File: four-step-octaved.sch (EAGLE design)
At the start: 29 parts, among them IC1 556, IC2 4017N, IC3 4040N, U1 LM386N

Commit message: Tighten
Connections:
- net +9V: no longer C4.1
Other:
- moved on the sheet: C4, IC2P, IC3, R1, RV1
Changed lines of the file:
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@@
 <instance part="IC1" gate="G$1" x="10.16" y="81.28"/>
 <instance part="IC2" gate="A" x="81.28" y="76.2"/>
-<instance part="IC3" gate="A" x="243.84" y="91.44"/>
+<instance part="IC3" gate="A" x="215.9" y="76.2"/>
 <instance part="U1" gate="G1" x="248.92" y="63.5"/>
 <instance part="SUPPLY1" gate="G$1" x="-25.4" y="101.6"/>
 <instance part="GND1" gate="1" x="-5.08" y="12.7"/>
-<instance part="R1" gate="G$1" x="-48.26" y="86.36"/>
+<instance part="R1" gate="G$1" x="-43.18" y="86.36"/>
 <instance part="R2" gate="G$1" x="-15.24" y="81.28" rot="R270"/>
 <instance part="R3" gate="G$1" x="35.56" y="81.28" rot="R90"/>
-<instance part="RV1" gate="G$1" x="-35.56" y="86.36" rot="R270"/>
+<instance part="RV1" gate="G$1" x="-30.48" y="86.36" rot="R270"/>
 <instance part="C1" gate="G$1" x="-15.24" y="68.58"/>
 <instance part="C2" gate="G$1" x="43.18" y="73.66"/>
@@
 <instance part="D7" gate="G$1" x="132.08" y="43.18"/>
 <instance part="D8" gate="G$1" x="154.94" y="35.56" rot="MR270"/>
-<instance part="IC2" gate="P" x="55.88" y="88.9" smashed="yes">
+<instance part="IC2" gate="P" x="60.96" y="86.36" smashed="yes">
 <attribute name="NAME" x="59.69" y="85.725" size="1.778" layer="95" rot="R90"/>
 </instance>
-<instance part="C4" gate="G$1" x="63.5" y="91.44"/>
+<instance part="C4" gate="G$1" x="66.04" y="86.36"/>
 </instances>
 <busses>
@@
 <pinref part="RV1" gate="G$1" pin="E"/>
 <wire x1="-2.54" y1="86.36" x2="-15.24" y2="86.36" width="0.1524" layer="91"/>
-<wire x1="-15.24" y1="86.36" x2="-27.94" y2="86.36" width="0.1524" layer="91"/>
-<wire x1="-27.94" y1="86.36" x2="-27.94" y2="81.28" width="0.1524" layer="91"/>
-<junction x="-27.94" y="86.36"/>
+<wire x1="-15.24" y1="86.36" x2="-22.86" y2="86.36" width="0.1524" layer="91"/>
+<wire x1="-22.86" y1="86.36" x2="-22.86" y2="81.28" width="0.1524" layer="91"/>
+<junction x="-22.86" y="86.36"/>
 <pinref part="RV1" gate="G$1" pin="S"/>
-<wire x1="-27.94" y1="81.28" x2="-35.56" y2="81.28" width="0.1524" layer="91"/>
+<wire x1="-22.86" y1="81.28" x2="-30.48" y2="81.28" width="0.1524" layer="91"/>
 <pinref part="R2" gate="G$1" pin="1"/>
 <junction x="-15.24" y="86.36"/>
@@
 <segment>
 <pinref part="SUPPLY1" gate="G$1" pin="+9V"/>
-<wire x1="-25.4" y1="99.06" x2="-58.42" y2="99.06" width="0.1524" layer="91"/>
-<wire x1="-58.42" y1="99.06" x2="-58.42" y2="86.36" width="0.1524" layer="91"/>
+<wire x1="-25.4" y1="99.06" x2="-50.8" y2="99.06" width="0.1524" layer="91"/>
+<wire x1="-50.8" y1="99.06" x2="-50.8" y2="86.36" width="0.1524" layer="91"/>
 <pinref part="R1" gate="G$1" pin="1"/>
-<wire x1="-58.42" y1="86.36" x2="-53.34" y2="86.36" width="0.1524" layer="91"/>
+<wire x1="-50.8" y1="86.36" x2="-48.26" y2="86.36" width="0.1524" layer="91"/>
 <pinref part="IC1" gate="G$1" pin="RST"/>
 <wire x1="-2.54" y1="78.74" x2="-7.62" y2="78.74" width="0.1524" layer="91"/>
@@
 <wire x1="43.18" y1="88.9" x2="43.18" y2="78.74" width="0.1524" layer="91"/>
 <junction x="25.4" y="88.9"/>
+<wire x1="25.4" y1="99.06" x2="60.96" y2="99.06" width="0.1524" layer="91"/>
+<junction x="25.4" y="99.06"/>
 <pinref part="IC2" gate="P" pin="VDD"/>
-<wire x1="25.4" y1="99.06" x2="55.88" y2="99.06" width="0.1524" layer="91"/>
-<wire x1="55.88" y1="99.06" x2="55.88" y2="96.52" width="0.1524" layer="91"/>
-<junction x="25.4" y="99.06"/>
-<pinref part="C4" gate="G$1" pin="1"/>
-<wire x1="63.5" y1="96.52" x2="55.88" y2="96.52" width="0.1524" layer="91"/>
-<junction x="55.88" y="96.52"/>
+<wire x1="60.96" y1="99.06" x2="60.96" y2="93.98" width="0.1524" layer="91"/>
 </segment>
 </net>
@@
 <pinref part="IC1" gate="G$1" pin="GND"/>
 <wire x1="-2.54" y1="71.12" x2="-5.08" y2="71.12" width="0.1524" layer="91"/>
-<wire x1="-5.08" y1="71.12" x2="-5.08" y2="60.96" width="0.1524" layer="91"/>
 <pinref part="GND1" gate="1" pin="GND"/>
-<pinref part="C1" gate="G$1" pin="-"/>
-<wire x1="-5.08" y1="60.96" x2="-5.08" y2="25.4" width="0.1524" layer="91"/>
+<wire x1="-5.08" y1="71.12" x2="-5.08" y2="25.4" width="0.1524" layer="91"/>
 <wire x1="-5.08" y1="25.4" x2="-5.08" y2="15.24" width="0.1524" layer="91"/>
-<wire x1="-15.24" y1="63.5" x2="-15.24" y2="60.96" width="0.1524" layer="91"/>
-<wire x1="-15.24" y1="60.96" x2="-5.08" y2="60.96" width="0.1524" layer="91"/>
-<junction x="-5.08" y="60.96"/>
-<pinref part="C3" gate="G$1" pin="2"/>
-<wire x1="35.56" y1="63.5" x2="35.56" y2="60.96" width="0.1524" layer="91"/>
-<wire x1="35.56" y1="60.96" x2="-5.08" y2="60.96" width="0.1524" layer="91"/>
-<junction x="-5.08" y="60.96"/>
-<pinref part="C2" gate="G$1" pin="2"/>
-<wire x1="43.18" y1="71.12" x2="43.18" y2="60.96" width="0.1524" layer="91"/>
-<wire x1="43.18" y1="60.96" x2="35.56" y2="60.96" width="0.1524" layer="91"/>
-<junction x="35.56" y="60.96"/>
 <pinref part="R4" gate="G$1" pin="1"/>
 <wire x1="66.04" y1="33.02" x2="66.04" y2="25.4" width="0.1524" layer="91"/>
-<wire x1="66.04" y1="25.4" x2="60.96" y2="25.4" width="0.1524" layer="91"/>
+<wire x1="66.04" y1="25.4" x2="63.5" y2="25.4" width="0.1524" layer="91"/>
 <junction x="-5.08" y="25.4"/>
 <pinref part="D2" gate="G$1" pin="C"/>
-<wire x1="60.96" y1="25.4" x2="55.88" y2="25.4" width="0.1524" layer="91"/>
-<wire x1="55.88" y1="25.4" x2="-5.08" y2="25.4" width="0.1524" layer="91"/>
+<wire x1="63.5" y1="25.4" x2="60.96" y2="25.4" width="0.1524" layer="91"/>
+<wire x1="60.96" y1="25.4" x2="43.18" y2="25.4" width="0.1524" layer="91"/>
+<wire x1="43.18" y1="25.4" x2="35.56" y2="25.4" width="0.1524" layer="91"/>
+<wire x1="35.56" y1="25.4" x2="-5.08" y2="25.4" width="0.1524" layer="91"/>
 <wire x1="160.02" y1="81.28" x2="162.56" y2="81.28" width="0.1524" layer="91"/>
 <wire x1="162.56" y1="81.28" x2="162.56" y2="66.04" width="0.1524" layer="91"/>
@@
 <pinref part="D8" gate="G$1" pin="C"/>
 <pinref part="C4" gate="G$1" pin="2"/>
-<wire x1="63.5" y1="88.9" x2="63.5" y2="81.28" width="0.1524" layer="91"/>
+<wire x1="66.04" y1="83.82" x2="66.04" y2="78.74" width="0.1524" layer="91"/>
 <pinref part="IC2" gate="P" pin="VSS"/>
-<wire x1="63.5" y1="81.28" x2="55.88" y2="81.28" width="0.1524" layer="91"/>
-<wire x1="55.88" y1="81.28" x2="55.88" y2="25.4" width="0.1524" layer="91"/>
-<junction x="55.88" y="81.28"/>
-<junction x="55.88" y="25.4"/>
+<wire x1="66.04" y1="78.74" x2="60.96" y2="78.74" width="0.1524" layer="91"/>
+<wire x1="60.96" y1="78.74" x2="60.96" y2="25.4" width="0.1524" layer="91"/>
+<junction x="60.96" y="78.74"/>
+<junction x="60.96" y="25.4"/>
 <pinref part="IC2" gate="A" pin="ENA"/>
-<wire x1="68.58" y1="66.04" x2="60.96" y2="66.04" width="0.1524" layer="91"/>
-<wire x1="60.96" y1="66.04" x2="60.96" y2="25.4" width="0.1524" layer="91"/>
-<junction x="60.96" y="25.4"/>
+<wire x1="68.58" y1="66.04" x2="63.5" y2="66.04" width="0.1524" layer="91"/>
+<wire x1="63.5" y1="66.04" x2="63.5" y2="25.4" width="0.1524" layer="91"/>
+<junction x="63.5" y="25.4"/>
+<pinref part="C1" gate="G$1" pin="-"/>
+<wire x1="-15.24" y1="63.5" x2="-15.24" y2="25.4" width="0.1524" layer="91"/>
+<wire x1="-15.24" y1="25.4" x2="-5.08" y2="25.4" width="0.1524" layer="91"/>
+<pinref part="C3" gate="G$1" pin="2"/>
+<wire x1="35.56" y1="63.5" x2="35.56" y2="25.4" width="0.1524" layer="91"/>
+<junction x="35.56" y="25.4"/>
+<pinref part="C2" gate="G$1" pin="2"/>
+<wire x1="43.18" y1="71.12" x2="43.18" y2="25.4" width="0.1524" layer="91"/>
+<junction x="43.18" y="25.4"/>
 </segment>
 </net>
@@
 <segment>
 <pinref part="IC1" gate="G$1" pin="OUT"/>
-<wire x1="-2.54" y1="76.2" x2="-25.4" y2="76.2" width="0.1524" layer="91"/>
-<wire x1="-25.4" y1="76.2" x2="-25.4" y2="55.88" width="0.1524" layer="91"/>
-<wire x1="-25.4" y1="55.88" x2="66.04" y2="55.88" width="0.1524" layer="91"/>
+<wire x1="-2.54" y1="76.2" x2="-22.86" y2="76.2" width="0.1524" layer="91"/>
+<wire x1="-22.86" y1="76.2" x2="-22.86" y2="55.88" width="0.1524" layer="91"/>
+<wire x1="-22.86" y1="55.88" x2="66.04" y2="55.88" width="0.1524" layer="91"/>
 <wire x1="66.04" y1="55.88" x2="66.04" y2="76.2" width="0.1524" layer="91"/>
 <pinref part="IC2" gate="A" pin="CLK"/>

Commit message: Add 4040 and 386
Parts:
- added C5: .1uF, SparkFun-Capacitors:0.1UF-KIT-EZ-50V-20%
- added C6: 220uF, SparkFun-Capacitors:100UF-POLAR-RADIAL-2.5MM-25V-20%
- added J1: SPEAKER, SparkFun-Connectors:CONN_02
- added R10, R9: 22K, SparkFun-Resistors:1KOHM-HORIZ-1/4W-1%
- added RV6: 1K, SparkFun-Retired:POTTRIM
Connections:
- new net N$20: IC3A.Q2, R9.2
- new net N$21: IC1.OUT2, IC3A.P1
- new net N$22: IC3A.Q3, R10.2
- new net N$23: R10.1, R9.1, RV6.A
- new net N$24: RV6.S, U1.+IN
- new net N$27: C6.-, J1.1
- new net N$28: C6.+, U1.OUT
- net +9V: now also C4.1, C5.1, IC3P.VDD, U1.V-
- net GND: now also C5.2, IC3A.RES, IC3P.VSS, J1.2, RV6.E, U1.-IN
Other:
- moved on the sheet: IC3, U1

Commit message: Cleanup and ERC
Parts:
- added J2: SPEAKER, SparkFun-Connectors:CONN_02
- C3: value 10uF -> 10nF
- J1: value SPEAKER -> BATTERY
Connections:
- net +9V: now also J1.1, U1.V+; no longer U1.V-
- net GND: now also J2.2, U1.V-
- net N$27: now also J2.1; no longer J1.1
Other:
- moved on the sheet: C3, C6, J1, R10, R3, U1

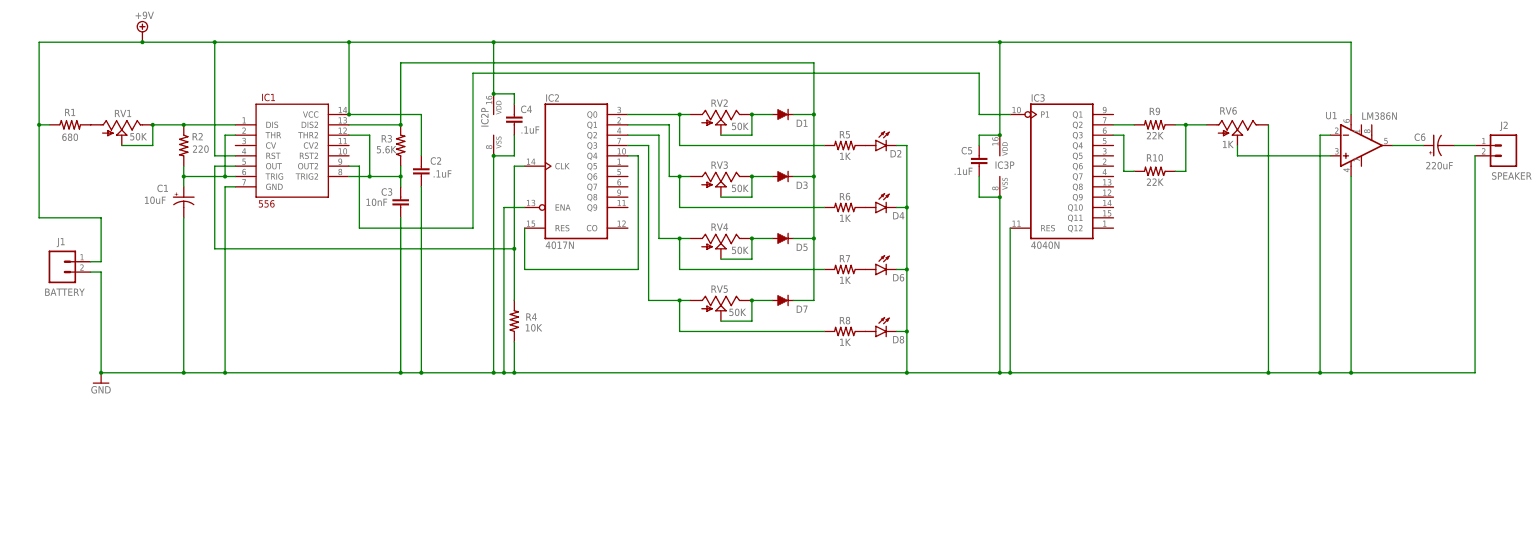
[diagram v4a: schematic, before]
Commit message: Shorten schematic to fit on one page
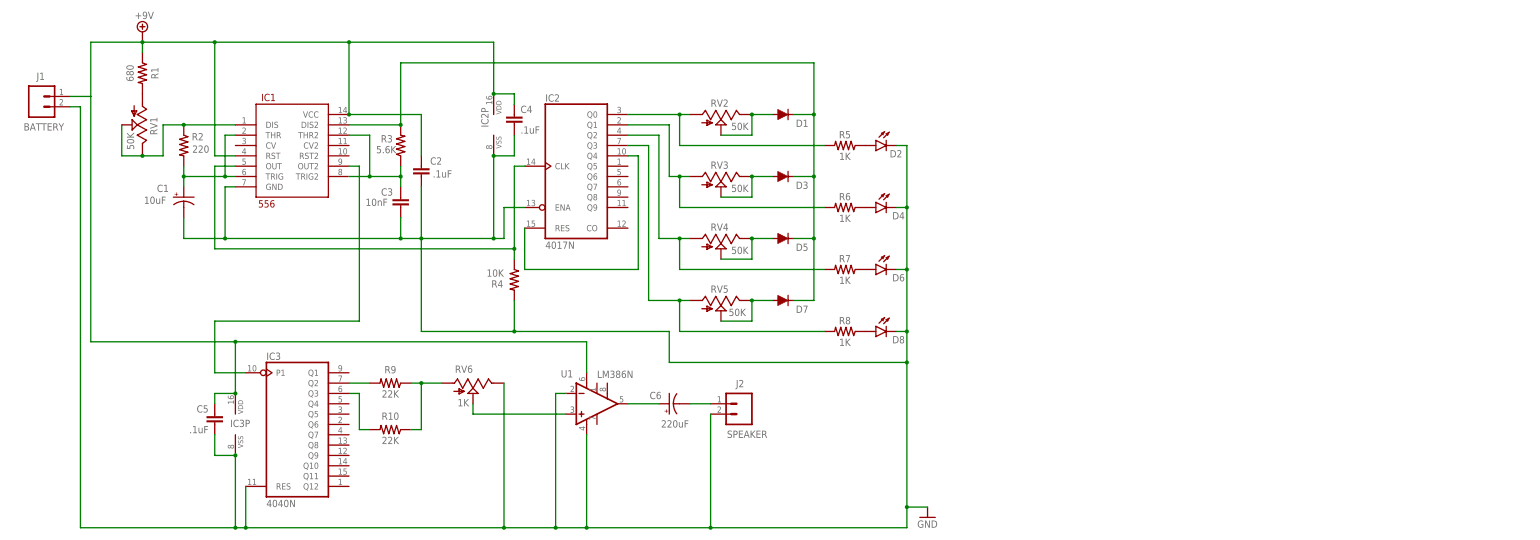
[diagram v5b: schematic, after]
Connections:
- net GND: now also R4.2; no longer R4.1
- net N$5: now also R4.1; no longer R4.2
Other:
- moved on the sheet: C5, C6, IC3, IC3P, J1, J2, R1, R10, R4, R9, RV1, RV6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
